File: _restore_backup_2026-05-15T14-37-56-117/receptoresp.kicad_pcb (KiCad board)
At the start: 2 copper layers, 48 x 59 mm, 7 parts

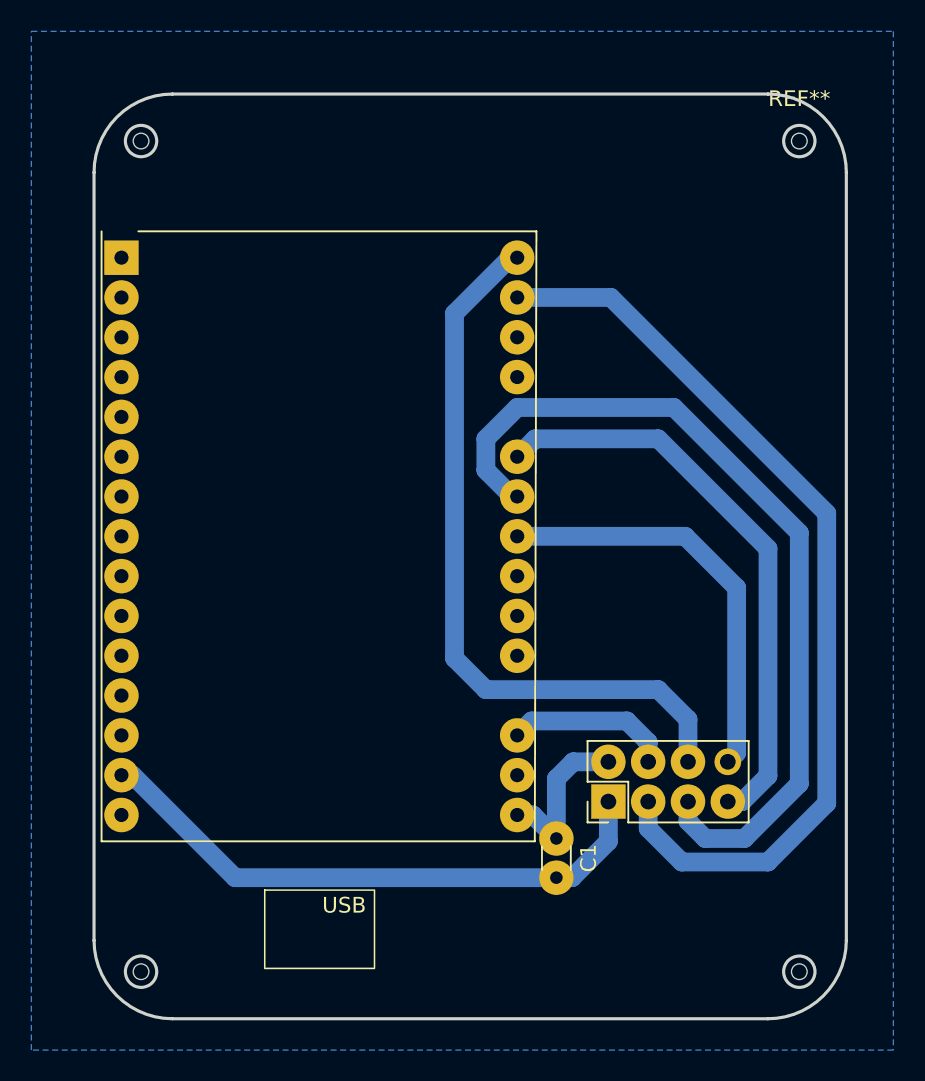
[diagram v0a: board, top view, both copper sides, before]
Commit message: capacitor polalizado 100uF
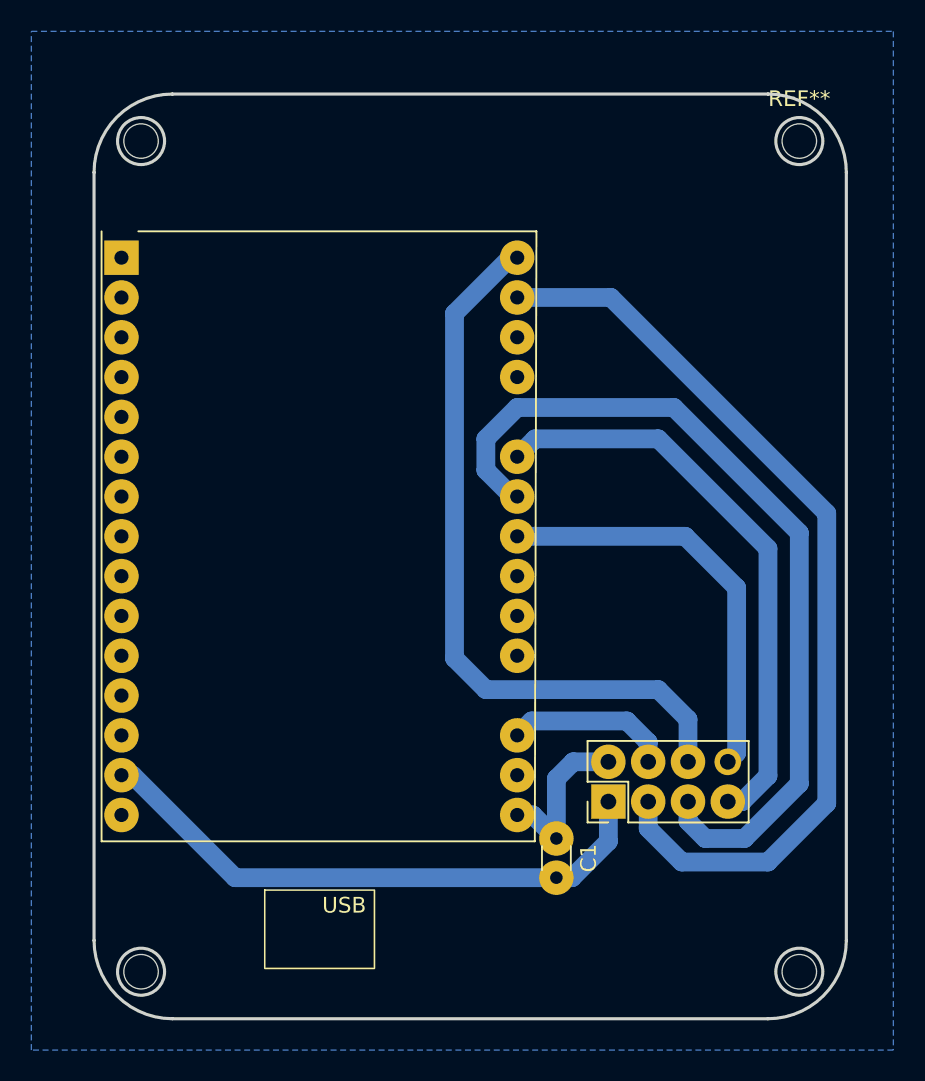
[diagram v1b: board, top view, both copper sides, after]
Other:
- outline, holes or cut-outs redrawn
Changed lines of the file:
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@@
 			(psa4output no)
 			(plot_black_and_white yes)
-			(sketchpadsonfab yes)
+			(sketchpadsonfab no)
 			(plotpadnumbers no)
 			(hidednponfab no)
@@
 			(drillshape 0)
 			(scaleselection 1)
-			(outputdirectory "../gerberpcb/")
+			(outputdirectory "/home/michelrochytor/Documentos/gerberpcb/")
 		)
 	)
@@
 		(pad "" np_thru_hole circle
 			(at 0 0)
-			(size 1 1)
-			(drill 1)
+			(size 2.2 2.2)
+			(drill 2.2)
 			(layers "*.Cu" "*.Mask")
 		)
@@
 		(pad "" np_thru_hole circle
 			(at 0 0)
-			(size 1 1)
-			(drill 1)
+			(size 2.2 2.2)
+			(drill 2.2)
 			(layers "*.Cu" "*.Mask")
 		)
@@
 		(pad "" np_thru_hole circle
 			(at 0 0)
-			(size 1 1)
-			(drill 1)
+			(size 2.2 2.2)
+			(drill 2.2)
 			(layers "*.Cu" "*.Mask")
 		)
@@
 		(attr exclude_from_pos_files exclude_from_bom)
 		(duplicate_pad_numbers_are_jumpers no)
+		(fp_circle
+			(center 0 0)
+			(end 1.75 0)
+			(stroke
+				(width 0.15)
+				(type solid)
+			)
+			(fill no)
+			(layer "Cmts.User")
+		)
+		(fp_circle
+			(center 0 0)
+			(end 2 0)
+			(stroke
+				(width 0.05)
+				(type solid)
+			)
+			(fill no)
+			(layer "F.CrtYd")
+		)
 		(fp_text user "${REFERENCE}"
-			(at 0 -1 0)
+			(at 0 0 0)
 			(layer "F.Fab")
 			(effects
@@
 		(pad "" np_thru_hole circle
 			(at 0 0)
-			(size 1 1)
-			(drill 1)
+			(size 2.2 2.2)
+			(drill 2.2)
 			(layers "*.Cu" "*.Mask")
 		)
@@
 	(gr_circle
 		(center 127 57)
-		(end 128 57)
+		(end 128.5 57)
 		(stroke
 			(width 0.2)
@@
 	(gr_circle
 		(center 127 110)
-		(end 128 110)
+		(end 128.5 110)
 		(stroke
 			(width 0.2)
@@
 	(gr_circle
 		(center 169 57)
-		(end 170 57)
+		(end 170.5 57)
 		(stroke
 			(width 0.2)
@@
 	(gr_circle
 		(center 169 110)
-		(end 170 110)
+		(end 170.5 110)
 		(stroke
 			(width 0.2)
